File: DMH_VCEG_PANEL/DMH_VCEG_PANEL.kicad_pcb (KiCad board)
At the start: 2 copper layers, 150 x 200 mm, 63 parts, among them J0 Panel_GND_Solder_Wire_Pad

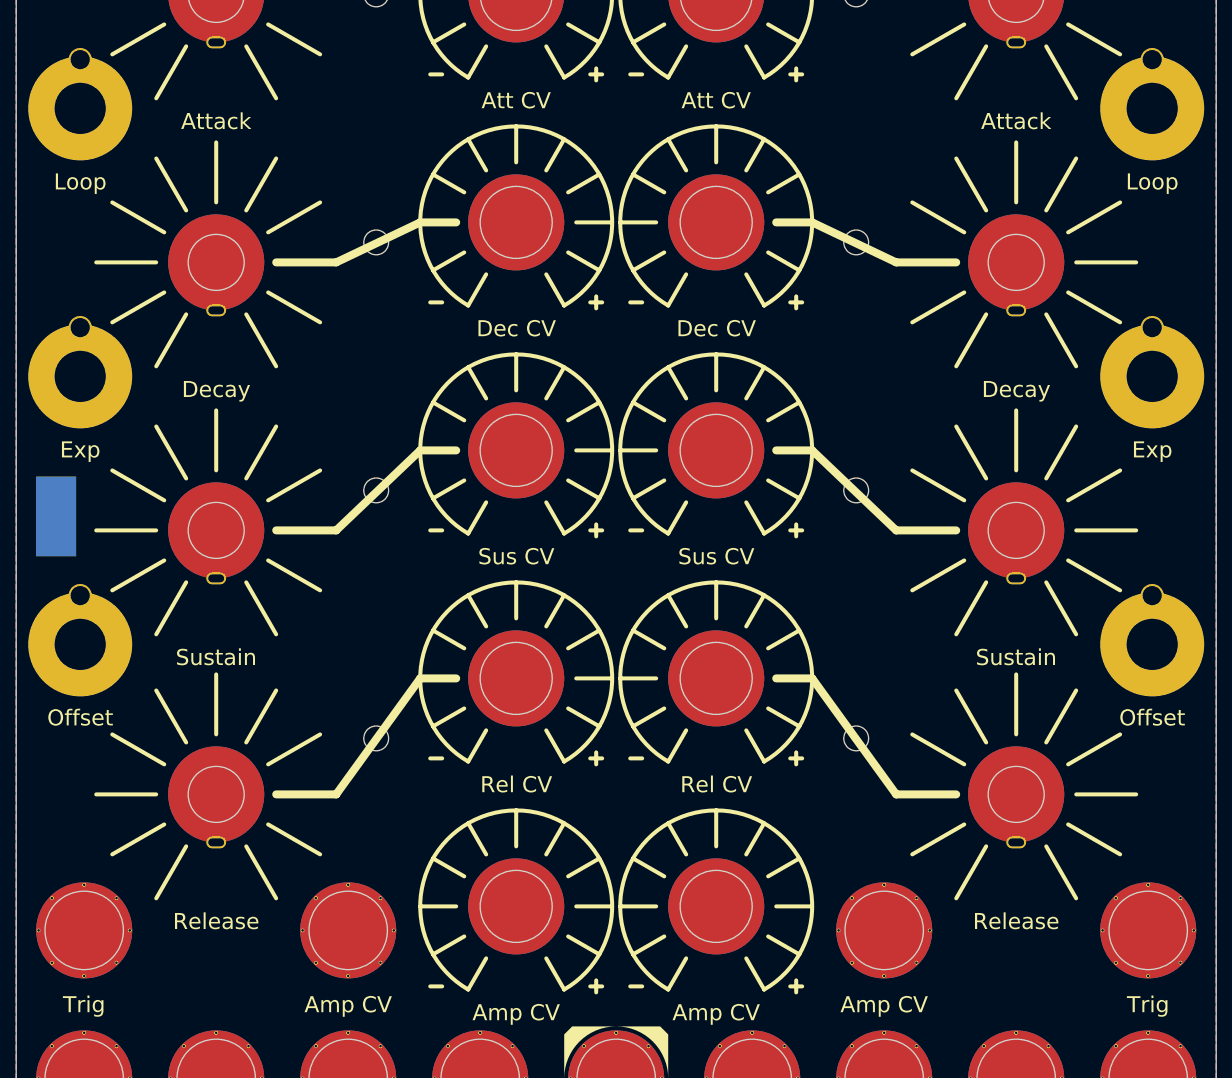
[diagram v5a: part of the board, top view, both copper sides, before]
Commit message: Removed built in VCA
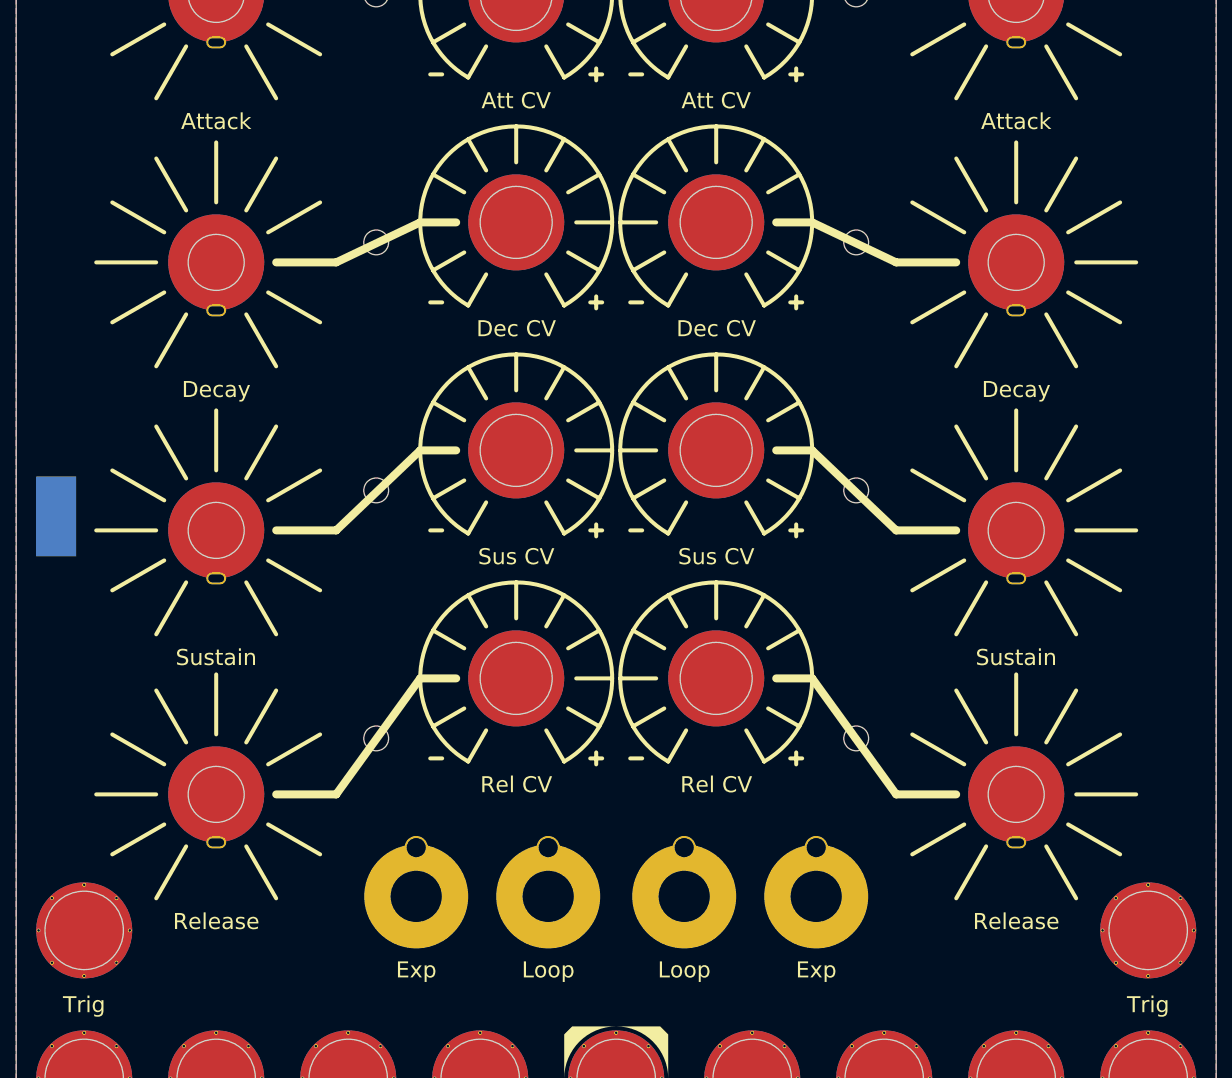
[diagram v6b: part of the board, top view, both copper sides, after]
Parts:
- removed H22, H45: Amp CV, SynthStuff:Jack_6.35mm_Cutout_v3
- removed H55, H56: Amp CV, SynthStuff:Pot_Cutout_Tiny_attv_P110KH1
- removed H57, H58: Offset, SynthStuff:Toggle_Switch_TE_Cutout
- moved H14 114.6 mm to (91.5, 167.5)
- moved H32 114.6 mm to (108.5, 167.5)
- moved H13 77.4 mm to (75.0, 167.5)
- moved H31 77.4 mm to (125.0, 167.5)

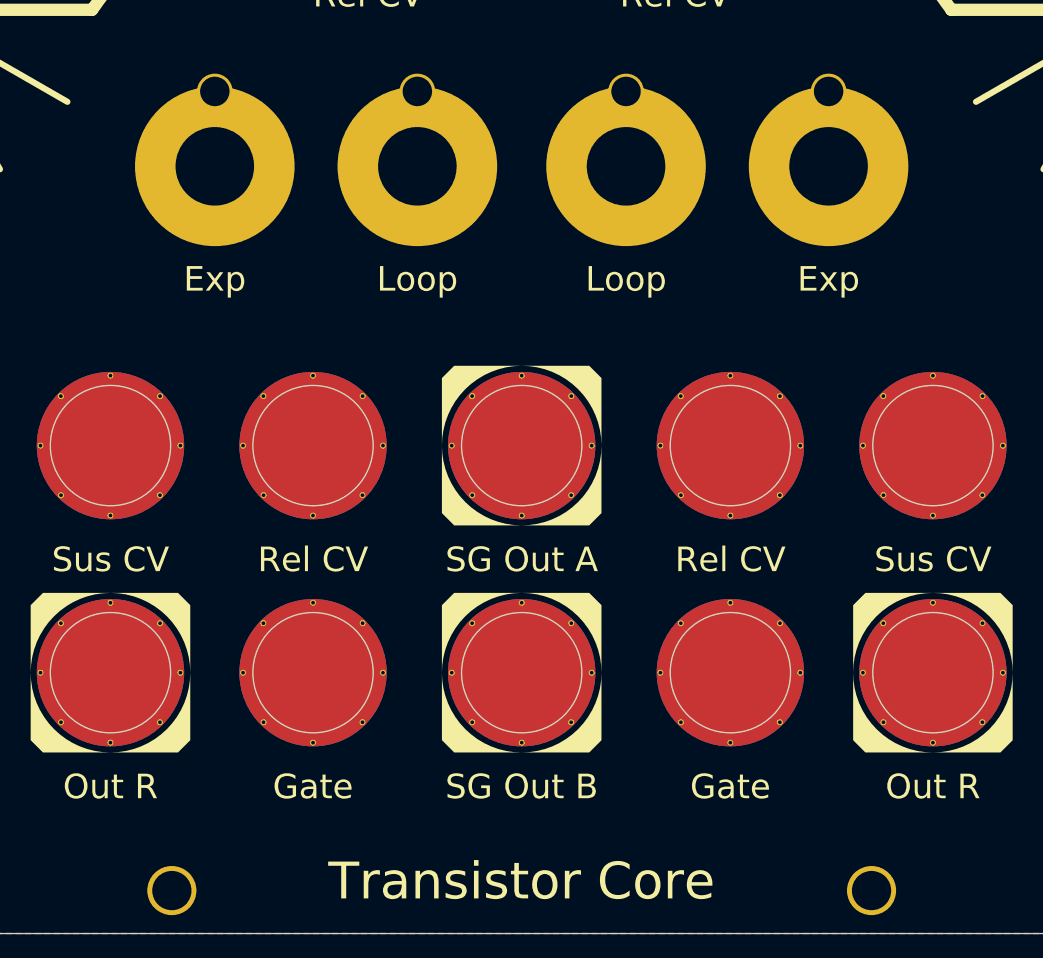
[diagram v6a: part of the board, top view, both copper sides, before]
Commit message: Updated Panel to new circuit
Changed Exp switch function to Long.
Added central switch to switch LEDs on and off.
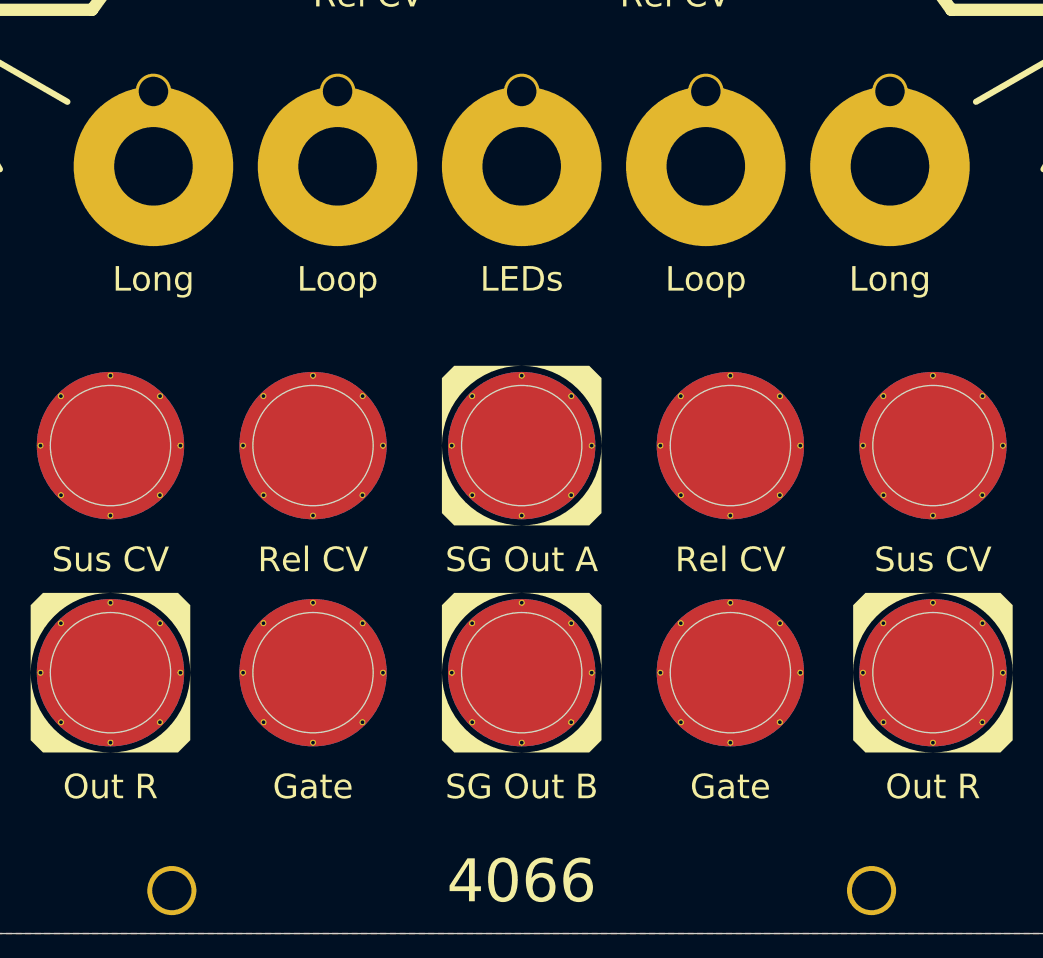
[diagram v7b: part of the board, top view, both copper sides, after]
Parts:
- added H45: LEDs, SynthStuff:Toggle_Switch_TE_Cutout, F.Cu at (100.0, 167.5)
- H13, H31: value Exp -> Long
- moved H14 6.50 mm to (85.0, 167.5)
- moved H32 6.50 mm to (115.0, 167.5)
- moved H13 5.00 mm to (70.0, 167.5)
- moved H31 5.00 mm to (130.0, 167.5)
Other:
- board text added: "4066"
- board text removed: "Transistor Core"
